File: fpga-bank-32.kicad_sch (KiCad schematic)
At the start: 1 part

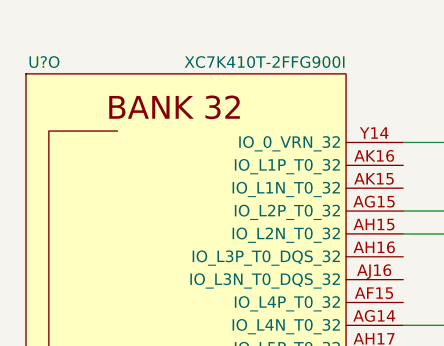
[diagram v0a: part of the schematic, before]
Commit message: Fix FPGA symbol
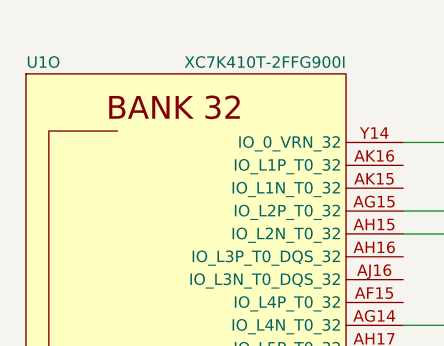
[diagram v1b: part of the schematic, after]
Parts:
- gave numbers to parts that had none: 1
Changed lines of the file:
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@@
     (effects (font (size 1.27 1.27)) (justify left))
   )
-  (symbol (lib_name "XC7K410T-2FFG900I_1") (lib_id "antmicroMicrocontrollers:XC7K410T-2FFG900I") (at 119.38 144.78 0) (unit 15)
+  (symbol (lib_id "antmicroMicrocontrollers:XC7K410T-2FFG900I") (at 119.38 144.78 0) (unit 15)
     (in_bom yes) (on_board yes)
-    (property "Reference" "U?" (id 0) (at 105.41 74.93 0)
+    (property "Reference" "U1" (id 0) (at 105.41 74.93 0)
       (effects (font (size 1.27 1.27)) (justify right))
     )

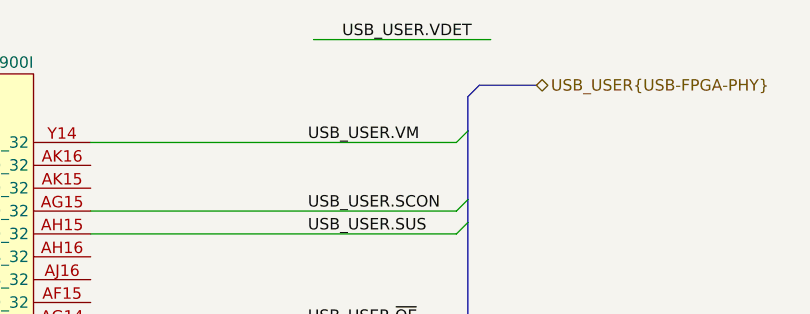
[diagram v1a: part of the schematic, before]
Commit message: Add fan headers
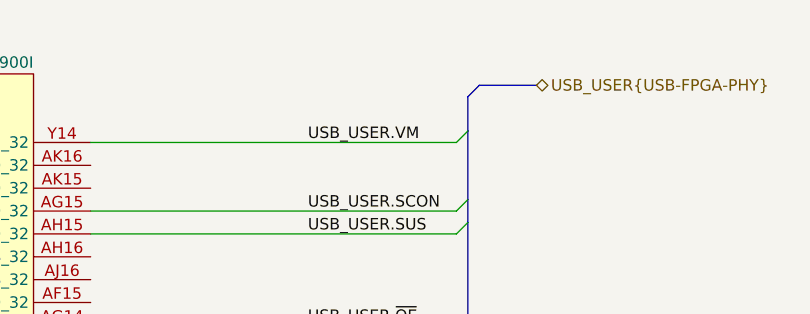
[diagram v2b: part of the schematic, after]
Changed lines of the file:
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@@
-    (stroke (width 0) (type default) (color 0 0 0 0))
-  )
-  (wire (pts (xy 187.96 72.39) (xy 168.275 72.39))
     (stroke (width 0) (type default) (color 0 0 0 0))
   )
@@
     (effects (font (size 1.27 1.27)) (justify left bottom))
   )
-  (label "USB_USER.VDET" (at 171.45 72.39 0)
-    (effects (font (size 1.27 1.27)) (justify left bottom))
-  )

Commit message: Loclib
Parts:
- U1: footprint antmicro-footprints:xc7k410t-2ffg900I -> K410T-devboard-footprints:xc7k410t-2ffg900I; symbol antmicroMicrocontrollers:XC7K410T-2FFG900I -> K410T-devboard:XC7K410T-2FFG900I
